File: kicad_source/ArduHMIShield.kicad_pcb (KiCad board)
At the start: 2 copper layers, 72 x 53 mm, 51 parts, among them CN1 ARDUINO_ISP, Q1 2N7002, SW1 TAST_VER, SW2 TAST_VER, SW3 TAST_VER, SW4 TAST_VER, SW5 TAST_VER, SW6 TAST_VER, U1 LT1117, U2 74VHC245D

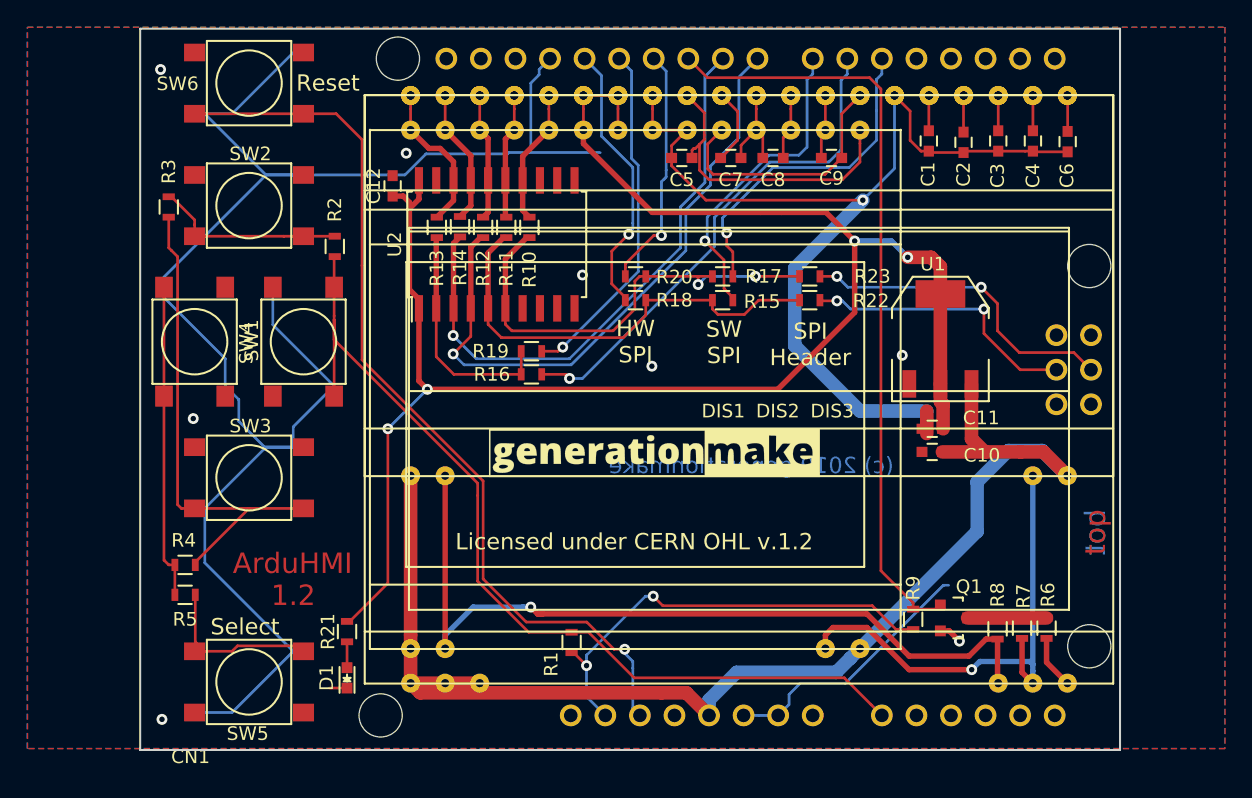
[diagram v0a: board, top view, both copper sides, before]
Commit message: added Arduino MKR conector
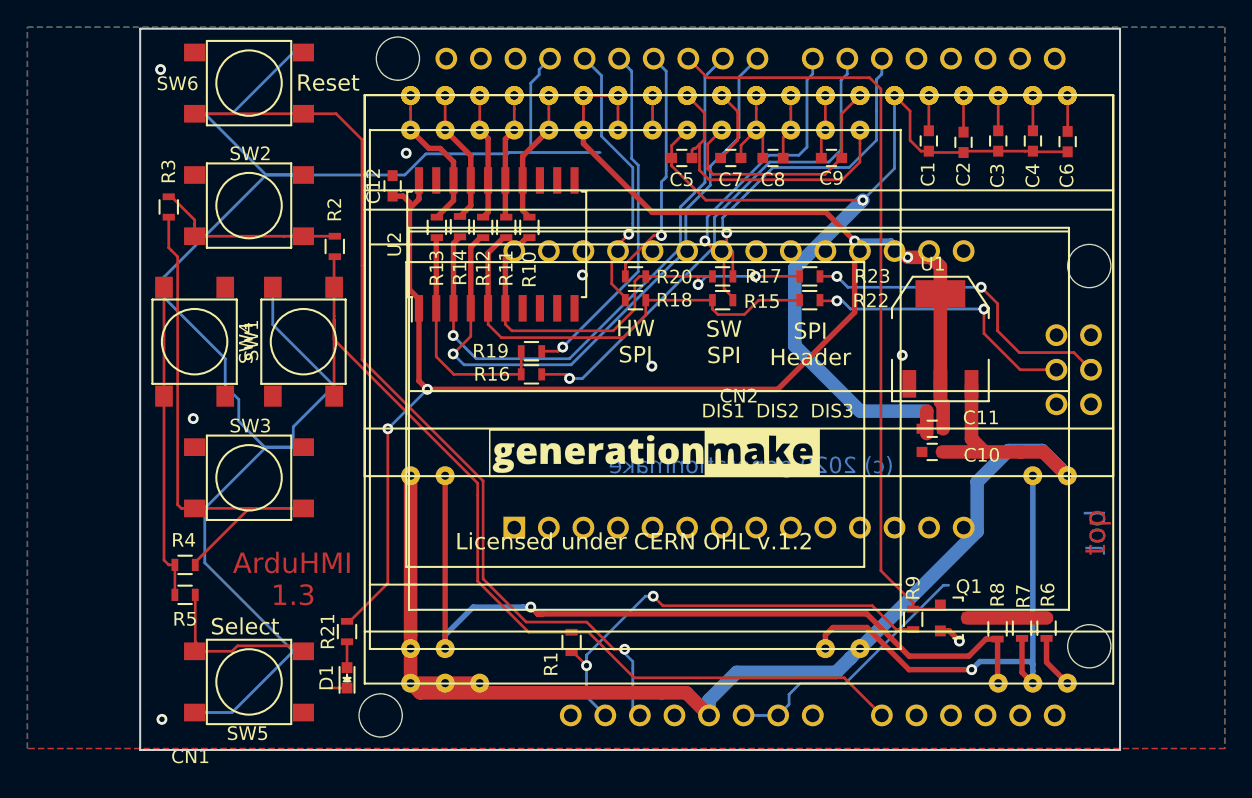
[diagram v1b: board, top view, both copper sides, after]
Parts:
- added CN2: ARDUINO_MKR, MODULE_compute:ARDUINO_MKR, F.Cu at (95.0, 103.5)
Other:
- board text added: "(c) 2020 generationmake"
- board text added: "1.3"
- board text removed: "(c) 2019 generationmake"
- board text removed: "1.2"

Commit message: updated layout
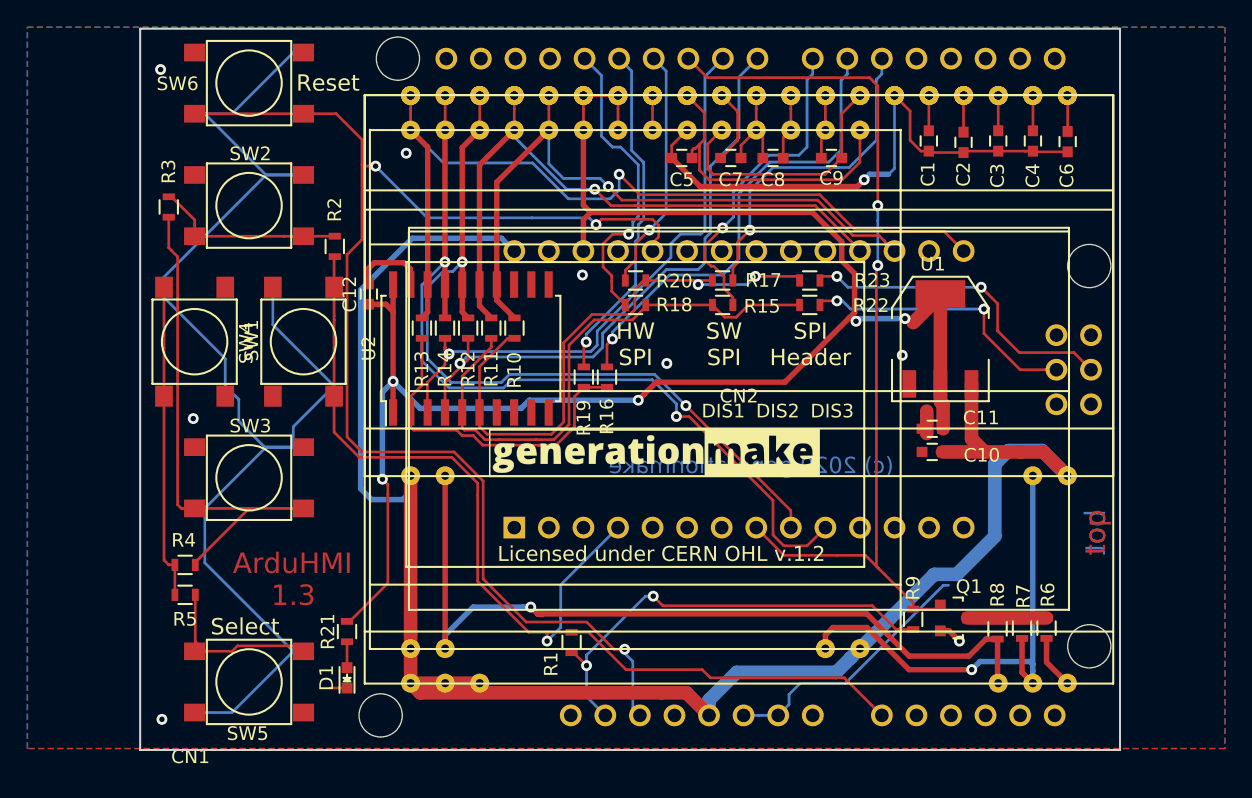
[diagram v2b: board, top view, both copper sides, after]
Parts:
- moved C12 8.14 mm to (67.8, 96.5)
- moved U2 7.88 mm to (75.3, 100.5)
- moved R14 7.53 mm to (73.4, 99.0)
- moved R11 7.48 mm to (76.8, 99.0)
- moved R12 7.48 mm to (75.1, 99.0)
- moved R10 7.48 mm to (78.5, 99.0)
- moved R13 7.48 mm to (71.7, 99.0)
- moved R16 5.55 mm to (85.3, 102.6), turned to 270 degrees
- moved G*** 4.56 mm to (104.5, 109.3)
- moved R19 4.29 mm to (83.6, 102.6), turned to 270 degrees
- moved R15 0.35 mm to (93.8, 97.3)
- moved R18 0.35 mm to (87.4, 97.3)
- moved R22 0.35 mm to (100.2, 97.3)
- moved R17 0.30 mm to (93.8, 95.5)
- moved R20 0.30 mm to (87.4, 95.5)
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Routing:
- net /DIS_RESET: track 10.0 -> 62.7 mm, vias 0 -> 2
- net /DIS_CS: track 11.2 -> 63.5 mm, vias 0 -> 1
- net GND: track 218.2 -> 167.3 mm
- net /DIS_A0: track 9.35 -> 58.7 mm, vias 0 -> 2
- net /DIS_SI: track 9.94 -> 49.0 mm, vias 0 -> 1
- net /DIS_CLK: track 9.24 -> 47.2 mm, vias 0 -> 1
- net +5V: track 115.6 -> 149.8 mm
- net /RESET: track 66.9 -> 97.8 mm, vias 1 -> 3
- net /DISPLAY_BL: track 56.4 -> 66.7 mm, vias 0 -> 2
- net /KEYPAD_A0: track 67.7 -> 77.2 mm, vias 0 -> 1
- net /ARDU_SI: track 33.8 -> 42.4 mm
- net /ARDU_CS: track 17.3 -> 24.9 mm
- net /ARDU_CLK: track 33.4 -> 40.8 mm
- net /ARDU_CS_2: track 37.2 -> 34.8 mm
- net /ARDU_CLK_1: track 20.3 -> 22.6 mm
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
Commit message: added holes for MKR connector
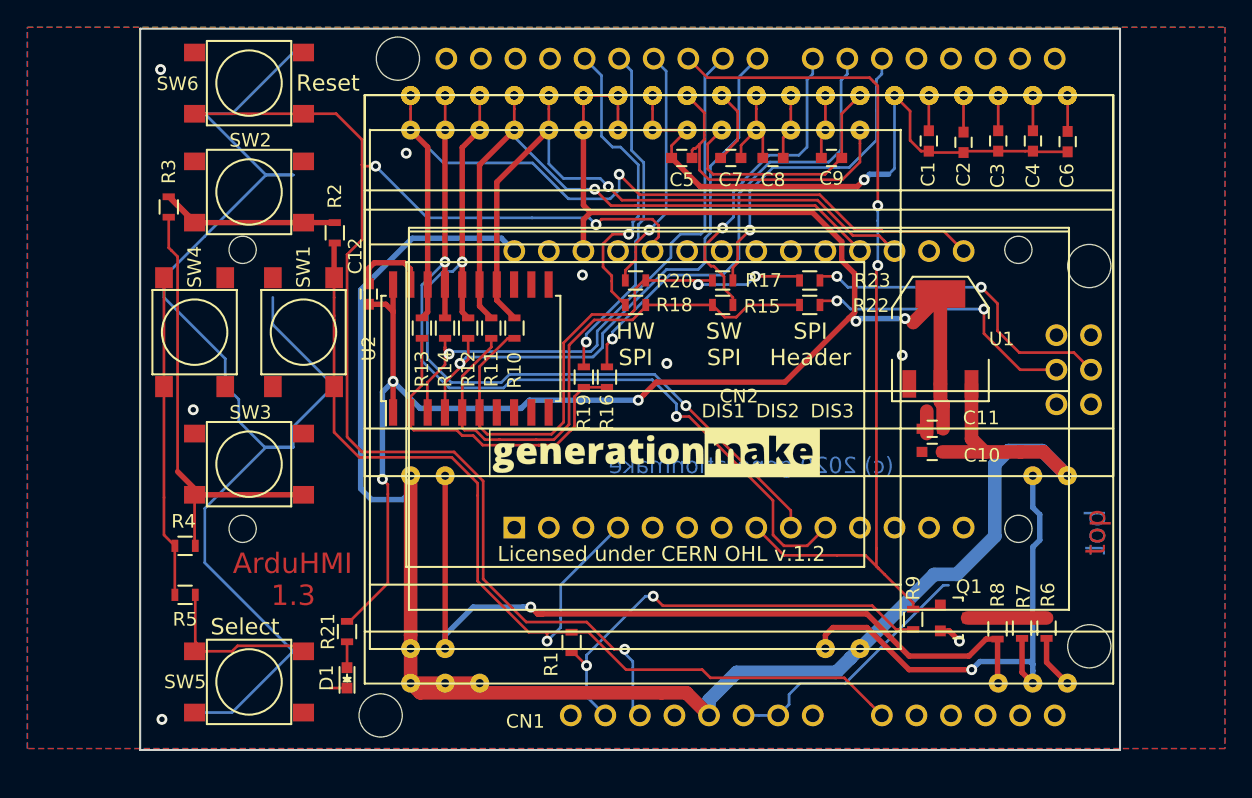
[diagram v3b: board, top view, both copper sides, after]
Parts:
- removed G*** (x2): generationmake_logo, labels:generationmake_logo
- added L1: Label, labels:generationmake_logo, B.Cu at (104.5, 109.3)
- added L2: Label, labels:generationmake_logo, F.Cu at (88.8, 113.5)
- CN2: footprint MODULE_compute:ARDUINO_MKR -> MODULE_compute:ARDUINO_MKR_HOLES
- moved R4 1.40 mm to (54.3, 115.0)
- moved R2 1.00 mm to (65.3, 92.0)
- moved SW2 1.00 mm to (59.0, 89.0)
- moved SW3 1.00 mm to (59.0, 109.0)
- moved SW1 0.70 mm to (63.0, 99.3)
- moved SW4 0.70 mm to (55.0, 99.3)
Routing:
- net /BUTTON_DOWN: track 35.8 -> 33.0 mm
- net /KEYPAD_A0: track 77.2 -> 79.8 mm
- net /BUTTON_UP: track 14.1 -> 15.9 mm
